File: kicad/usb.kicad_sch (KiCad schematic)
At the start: 39 parts, among them J5 xSYS2, J6 USB_C_Receptacle_USB2.0_16P, U10 W25Q32JVSS, U21 XU316-1024-QF60B-C24, Y2 TKC 7M 24MHz

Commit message: #11
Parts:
- removed C100, C101, C102, C104, C105, C71, C74, C75, C80, C83, C90, C95, C96, C97, C98, C99: 100nF, symbol Device:C_Small
- removed C103: 10uF, symbol Device:C_Small
- removed C63, C69: 22pF, symbol Device:C_Small
- removed C70: 1uF, symbol Device:C_Small
- removed FB1: 600R, symbol Device:FerriteBead_Small
- removed J6: USB_C_Receptacle_USB2.0_16P, symbol Connector:USB_C_Receptacle_USB2.0_16P
- removed R40: 1M, symbol Device:R_Small_US
- removed R41: 30, symbol Device:R_Small_US
- removed R53, R54: 43, symbol Device:R_Small_US
- removed R56, R57: 5k1, symbol Device:R_Small_US
- removed R58, R59, R60, R61: 47k, symbol Device:R_Small_US
- removed U21: XU316-1024-QF60B-C24, QFN_F60B-C24_XMO, symbol openmic:XU316-1024-QF60B-C24_1
- removed Y2: TKC 7M 24MHz, symbol Device:Crystal_GND24_Small
- added C139, C140, C141, C142, C143, C144, C145, C146, C147, C148, C149, C150, C151, C152, C153, C154, C155, C156, C157, C158, C159, C163, C164, C166, C29, C30: 100nF, symbol Device:C_Small
- added C160, C161: 22pF, symbol Device:C_Small
- added C162: 1uF, symbol Device:C_Small
- added C165: 10uF, symbol Device:C_Small
- added FB2: 600R, symbol Device:FerriteBead_Small
- added J3: USB_C_Receptacle_USB2.0_16P, symbol Connector:USB_C_Receptacle_USB2.0_16P
- added R1, R32: 5k1, symbol Device:R_Small_US
- added R110, R111, R63: 47k, symbol Device:R_Small_US
- added R64: 30, symbol Device:R_Small_US
- added R65: 1M, symbol Device:R_Small_US
- added U6: XU316-1024-TQ128-C24, XU316-1024-TQ128-C24:QFP40P1600X1600X120-129N, symbol openmic:XU316-1024-TQ128-C24
- added Y1: TKC 7M 24MHz, symbol Device:Crystal_GND24_Small
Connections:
- net +0V9: now also C139.1, C140.1, C141.1, C142.1, C143.1, C144.1, C145.1, C146.1, C147.1, C148.1, C149.1, C150.1, C151.1, C29.1, C30.1, FB2.2, U6.104 (VDD__11), U6.105 (VDD__12), U6.106 (VDD__13), U6.11 (VDD__1), U6.113 (VDD__14), U6.14 (VDD__2), U6.18 (VDD__3), U6.39 (VDD__4), U6.45 (VDD__5), U6.5 (VDD), U6.50 (VDD__6), U6.54 (VDD__7), U6.68 (VDD__8), U6.85 (VDD__9), U6.95 (VDD__10)
- net +1V8: now also C158.1, C159.1, C163.1, U6.35 (VDDIOB18), U6.56 (VDDIOB18__1), U6.62 (USB_VDD18)
- net +3V3: now also C152.1, C153.1, C154.1, C155.1, C156.1, C157.1, C164.1, R110.1, R111.1, R63.1, U6.10 (VDDIOL), U6.109 (VDDIOT), U6.121 (VDDIOT__1), U6.17 (VDDIOL__1), U6.61 (USB_VDD33), U6.72 (VDDIOR), U6.89 (VDDIOR__1)
- net +5V_USB: now also C165.2, C166.1, J3.A4 (VBUS), J3.A9 (VBUS), J3.B4 (VBUS), J3.B9 (VBUS)
- net CS_1: now also R110.2, U6.90 (X0D27)
- net Earth: now also J3.S1 (SHIELD)
- net GNDD: now also C139.2, C140.2, C141.2, C142.2, C143.2, C144.2, C145.2, C146.2, C147.2, C148.2, C149.2, C150.2, C151.2, C152.2, C153.2, C154.2, C155.2, C156.2, C157.2, C158.2, C159.2, C160.1, C161.1, C162.2, C163.2, C164.2, C165.1, C166.2, C29.2, C30.2, J3.A1 (GND), J3.A12 (GND), J3.B1 (GND), J3.B12 (GND), R1.2, R32.1, U6.129 (VSS__1), U6.24 (MIPI_VDD18), U6.27 (MIPI_VDD09), U6.30 (VSS), U6.42 (PLL_AGND), Y1.2 (G), Y1.4 (G)
- net I2S_BCLK: now also U6.19 (X1D00)
- net I2S_FSYNC: now also U6.20 (X1D01)
- net I2S_MCLK: now also U6.22 (X1D10)
- net I2S_SDIN: now also U6.53 (X1D12)
- net I2S_SDOUT: now also U6.23 (X1D11)
- net JTAG_TCK: now also U6.51 (TCK)
- net JTAG_TDI: now also U6.36 (TDI)
- net JTAG_TDO: now also U6.37 (TDO)
- net JTAG_TMS: now also U6.44 (TMS)
- net PH_EN: now also U6.91 (X0D28)
- net PH_IND: now also U6.98 (X0D40)
- net QSPI_CS: now also R63.2, U6.2 (X0D01)
- net QSPI_SCLK: now also U6.4 (X0D10)
- net QSPI_SPIO0: now also U6.127 (X0D04)
- net QSPI_SPIO1: now also U6.128 (X0D05)
- net QSPI_SPIO2: now also U6.1 (X0D06)
- net QSPI_SPIO3: now also U6.3 (X0D07)
- net ROT_A_1: now also U6.86 (X0D24)
- net ROT_A_2: now also U6.125 (X0D34)
- net ROT_B_1: now also U6.87 (X0D25)
- net ROT_B_2: now also U6.93 (X0D35)
- net RST_N: now also U6.38 (~{RST})
- net SPI_DIN: now also U6.7 (X0D11)
- net SPI_DOUT: now also U6.46 (X0D12)
- net SPI_SCLK: now also U6.47 (X0D13)
- net XL0_IN_0: now also U6.67 (X1D17)
- net XL0_IN_1: now also U6.66 (X1D16)
- net XL0_OUT_0: now also U6.69 (X1D18)
- net XL0_OUT_1: now also U6.70 (X1D19)
- new net: C160.2, R64.1, Y1.3
- new net: J3.A5 (CC1), R1.1
- new net: R64.2, R65.1, U6.33 (XOUT)
- new net: C161.2, R65.2, U6.34 (XIN), Y1.1
- new net: J3.A7 (D-), J3.B7 (D-), U6.59 (USB_DM)
- new net: J3.A6 (D+), J3.B6 (D+), U6.60 (USB_DP)
- new net: J3.B5 (CC2), R32.2
- new net CS_0: R111.2, U6.88 (X0D26)
- new net GP0_1A: U6.6 (X0D00)
- new net GP0_4C_0: U6.8 (X0D14)
- new net GP0_4D_0: U6.9 (X0D16)
- new net GP1_1F: U6.64 (X1D13)
- new net GP1_1G: U6.74 (X1D22)
- new net GP1_1H: U6.57 (X1D23)
- new net GP1_1I: U6.107 (X1D24)
- new net GP1_1J: U6.108 (X1D25)
- new net GP1_1K: U6.119 (X1D34)
- new net GP1_1L: U6.120 (X1D35)
- new net GP1_1M: U6.12 (X1D36)
- new net GP1_1N: U6.13 (X1D37)
- new net GP1_1O: U6.15 (X1D38)
- new net GP1_1P: U6.16 (X1D39)
- new net GP1_32A_0: U6.75 (X1D49)
- new net GP1_32A_1: U6.76 (X1D50)
- new net GP1_32A_2: U6.77 (X1D51)
- new net GP1_32A_3: U6.78 (X1D52)
- new net GP1_32A_4: U6.79 (X1D53)
- new net GP1_32A_5: U6.80 (X1D54)
- new net GP1_32A_6: U6.81 (X1D55)
- new net GP1_32A_7: U6.82 (X1D56)
- new net GP1_32A_8: U6.83 (X1D57)
- new net GP1_32A_9: U6.84 (X1D58)
- new net GP1_4A_3: U6.21 (X1D09)
- new net GP1_4C_0: U6.63 (X1D14)
- new net GP1_4C_1: U6.65 (X1D15)
- new net GP1_4C_2: U6.71 (X1D20)
- new net GP1_4C_3: U6.73 (X1D21)
- new net GP1_4E_0: U6.110 (X1D26)
- new net GP1_4E_1: U6.111 (X1D27)
- new net GP1_4E_2: U6.117 (X1D32)
- new net GP1_4E_3: U6.118 (X1D33)
- new net GP1_4F_0: U6.112 (X1D28)
- new net GP1_4F_1: U6.114 (X1D29)
- new net GP1_4F_2: U6.115 (X1D30)
- new net GP1_4F_3: U6.116 (X1D31)
- new net GP1_8D_7: U6.102 (X1D43)
- new net GPO_3: U6.92 (X0D29)
- new net GPO_4: U6.122 (X0D30)
- new net GPO_5: U6.124 (X0D31)
- new net GPO_6: U6.123 (X0D32)
- new net GPO_7: U6.126 (X0D33)
- new net IND_1: U6.101 (X0D41)
- new net IND_2: U6.100 (X0D42)
- new net IND_3: U6.103 (X0D43)
- new net PLL_AVDD: C162.1, FB2.1, U6.41 (PLL_AVDD)
- new net ROT_A_0: U6.48 (X0D22)
- new net ROT_A_3: U6.94 (X0D36)
- new net ROT_A_4: U6.97 (X0D38)
- new net ROT_B_0: U6.49 (X0D23)
- new net ROT_B_3: U6.96 (X0D37)
- new net ROT_B_4: U6.99 (X0D39)
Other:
- note added: "leave floating for 3V3"
- moved on the sheet: C81, C82, J5, R55, U10

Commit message: tac5212 initial architecture
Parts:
- added R56: 47k, symbol Device:R_Small_US
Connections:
- net GPO_3 is gone; now on net PH_EN: U6.92 (X0D29)
- net +3V3: now also R56.1
- net PH_EN: no longer U6.91 (X0D28)
- new net CS_2: R56.2, U6.91 (X0D28)
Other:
- moved on the sheet: R110, R111, U10

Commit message: #14
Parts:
- added U7: 74AHCT125, symbol 74xx:74AHCT125
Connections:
- net GNDD: now also U7.7 (GND)
- net GP0_1A: now also U7.2
- new net +5V: U7.1, U7.14 (VCC)
- new net LED_CONTROL: U7.3
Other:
- moved on the sheet: R63, U10

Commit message: phones out
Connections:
- net GPO_4 renamed PHONES_EN
- net IND_1 renamed PHONES_IND
- net IND_2 renamed LINE_IND_L
- net IND_3 renamed LINE_IND_R
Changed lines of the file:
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@@
 		)
 	)
-	(hierarchical_label "IND_2"
+	(hierarchical_label "LINE_IND_L"
 		(shape input)
 		(at 92.71 146.05 180)
@@
 		)
 	)
-	(hierarchical_label "IND_1"
+	(hierarchical_label "PHONES_IND"
 		(shape input)
 		(at 92.71 143.51 180)
@@
 		)
 	)
-	(hierarchical_label "GPO_4"
+	(hierarchical_label "PHONES_EN"
 		(shape output)
 		(at 92.71 115.57 180)
@@
 		)
 	)
-	(hierarchical_label "IND_3"
+	(hierarchical_label "LINE_IND_R"
 		(shape input)
 		(at 92.71 148.59 180)

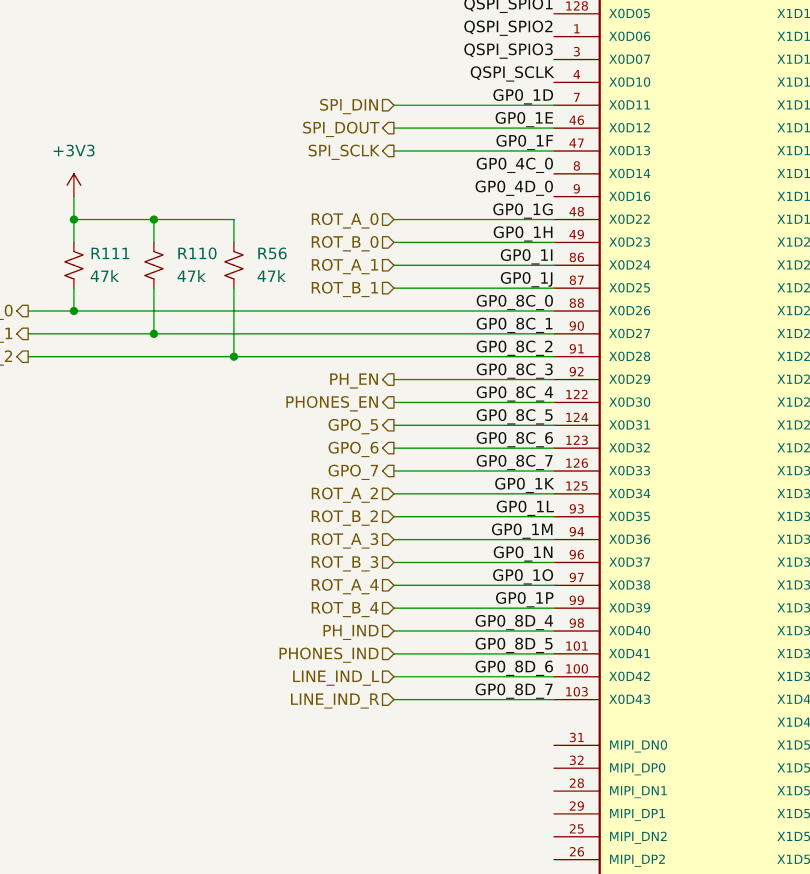
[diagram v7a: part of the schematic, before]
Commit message: monitor switch
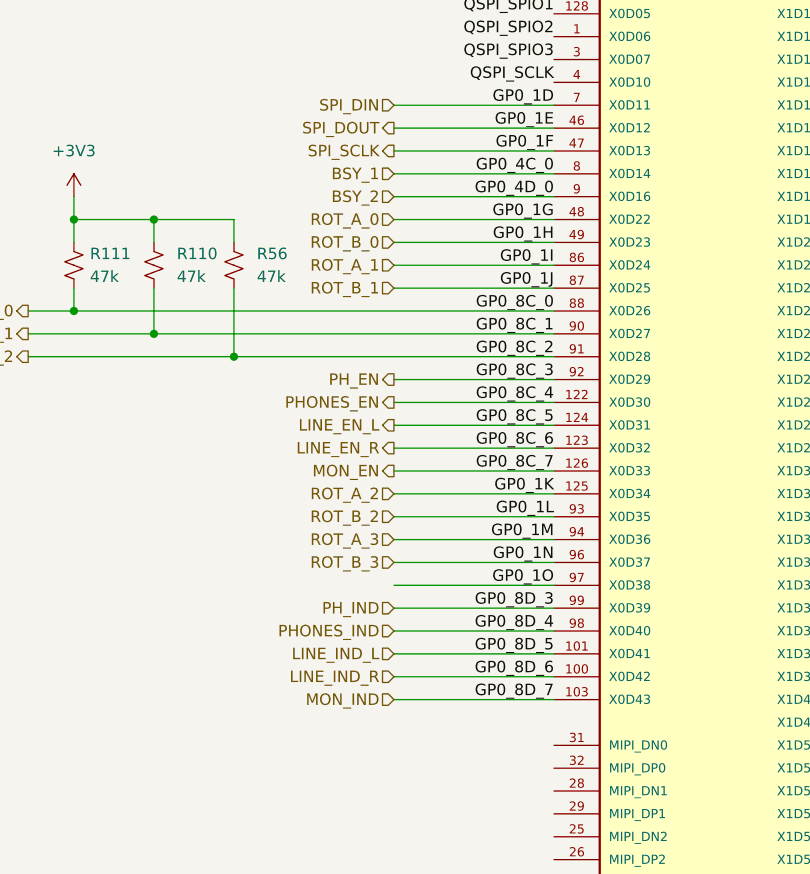
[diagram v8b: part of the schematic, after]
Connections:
- net ROT_B_4 is gone; now on net PH_IND: U6.99 (X0D39)
- net LINE_IND_L: now also U6.101 (X0D41); no longer U6.100 (X0D42)
- net LINE_IND_R: now also U6.100 (X0D42); no longer U6.103 (X0D43)
- net PHONES_IND: now also U6.98 (X0D40); no longer U6.101 (X0D41)
- net PH_IND: no longer U6.98 (X0D40)
- net GP0_4C_0 renamed BSY_1
- net GP0_4D_0 renamed BSY_2
- net GPO_5 renamed LINE_EN_L
- net GPO_6 renamed LINE_EN_R
- net GPO_7 renamed MON_EN
- net ROT_A_4 renamed GP0_1O
- new net MON_IND: U6.103 (X0D43)
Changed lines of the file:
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@@
+	(wire
+		(pts
+			(xy 92.71 92.71) (xy 110.49 92.71)
+		)
+		(stroke
+			(width 0)
+			(type default)
+		)
+	)
 	(wire
 		(pts
@@
 		(pts
 			(xy 52.07 110.49) (xy 74.93 110.49)
+		)
+		(stroke
+			(width 0)
+			(type default)
+		)
+	)
+	(wire
+		(pts
+			(xy 92.71 90.17) (xy 110.49 90.17)
 		)
 		(stroke
@@
 		)
 	)
-	(label "GP0_1P"
+	(label "GP0_8D_3"
 		(at 110.49 138.43 180)
 		(effects
@@
 			)
 			(justify right bottom)
-		)
-	)
-	(hierarchical_label "LINE_IND_L"
-		(shape input)
-		(at 92.71 146.05 180)
-		(effects
-			(font
-				(size 1.27 1.27)
-			)
-			(justify right)
 		)
 	)
@@
 		)
 	)
-	(hierarchical_label "PHONES_IND"
-		(shape input)
-		(at 92.71 143.51 180)
-		(effects
-			(font
-				(size 1.27 1.27)
-			)
-			(justify right)
-		)
-	)
 	(hierarchical_label "ROT_A_2"
 		(shape input)
@@
 		)
 	)
+	(hierarchical_label "PH_IND"
+		(shape input)
+		(at 92.71 138.43 180)
+		(effects
+			(font
+				(size 1.27 1.27)
+			)
+			(justify right)
+		)
+	)
+	(hierarchical_label "PHONES_IND"
+		(shape input)
+		(at 92.71 140.97 180)
+		(effects
+			(font
+				(size 1.27 1.27)
+			)
+			(justify right)
+		)
+	)
 	(hierarchical_label "ROT_B_2"
 		(shape input)
@@
 		)
 	)
+	(hierarchical_label "BSY_1"
+		(shape input)
+		(at 92.71 90.17 180)
+		(effects
+			(font
+				(size 1.27 1.27)
+			)
+			(justify right)
+		)
+	)
+	(hierarchical_label "MON_IND"
+		(shape input)
+		(at 92.71 148.59 180)
+		(effects
+			(font
+				(size 1.27 1.27)
+			)
+			(justify right)
+		)
+	)
 	(hierarchical_label "I2S_SDIN"
 		(shape input)
@@
 		)
 	)
-	(hierarchical_label "GPO_5"
+	(hierarchical_label "LINE_EN_L"
 		(shape output)
 		(at 92.71 118.11 180)
-		(effects
-			(font
-				(size 1.27 1.27)
-			)
-			(justify right)
-		)
-	)
-	(hierarchical_label "ROT_B_4"
-		(shape input)
-		(at 92.71 138.43 180)
 		(effects
 			(font
@@
 		)
 	)
-	(hierarchical_label "GPO_6"
+	(hierarchical_label "LINE_EN_R"
 		(shape output)
 		(at 92.71 120.65 180)
@@
 		)
 	)
-	(hierarchical_label "ROT_A_4"
+	(hierarchical_label "BSY_2"
 		(shape input)
-		(at 92.71 135.89 180)
+		(at 92.71 92.71 180)
 		(effects
 			(font
@@
 		)
 	)
-	(hierarchical_label "GPO_7"
+	(hierarchical_label "MON_EN"
 		(shape output)
 		(at 92.71 123.19 180)
@@
 		)
 	)
+	(hierarchical_label "LINE_IND_L"
+		(shape input)
+		(at 92.71 143.51 180)
+		(effects
+			(font
+				(size 1.27 1.27)
+			)
+			(justify right)
+		)
+	)
 	(hierarchical_label "ROT_B_0"
 		(shape input)
@@
 		)
 	)
+	(hierarchical_label "LINE_IND_R"
+		(shape input)
+		(at 92.71 146.05 180)
+		(effects
+			(font
+				(size 1.27 1.27)
+			)
+			(justify right)
+		)
+	)
 	(hierarchical_label "ROT_B_1"
 		(shape input)
@@
 		(effects
 			(font
-				(size 1.27 1.27)
-			)
-			(justify right)
-		)
-	)
-	(hierarchical_label "LINE_IND_R"
-		(shape input)
-		(at 92.71 148.59 180)
-		(effects
-			(font
-				(size 1.27 1.27)
-			)
-			(justify right)
-		)
-	)
-	(hierarchical_label "PH_IND"
-		(shape input)
-		(at 92.71 140.97 180)
-		(effects
-			(font
